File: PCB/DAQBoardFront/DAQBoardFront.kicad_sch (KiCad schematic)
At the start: 35 parts, among them IC2 LMR51430YDDCR, J2 53375-0410, U5 TCAN1051VDRQ1

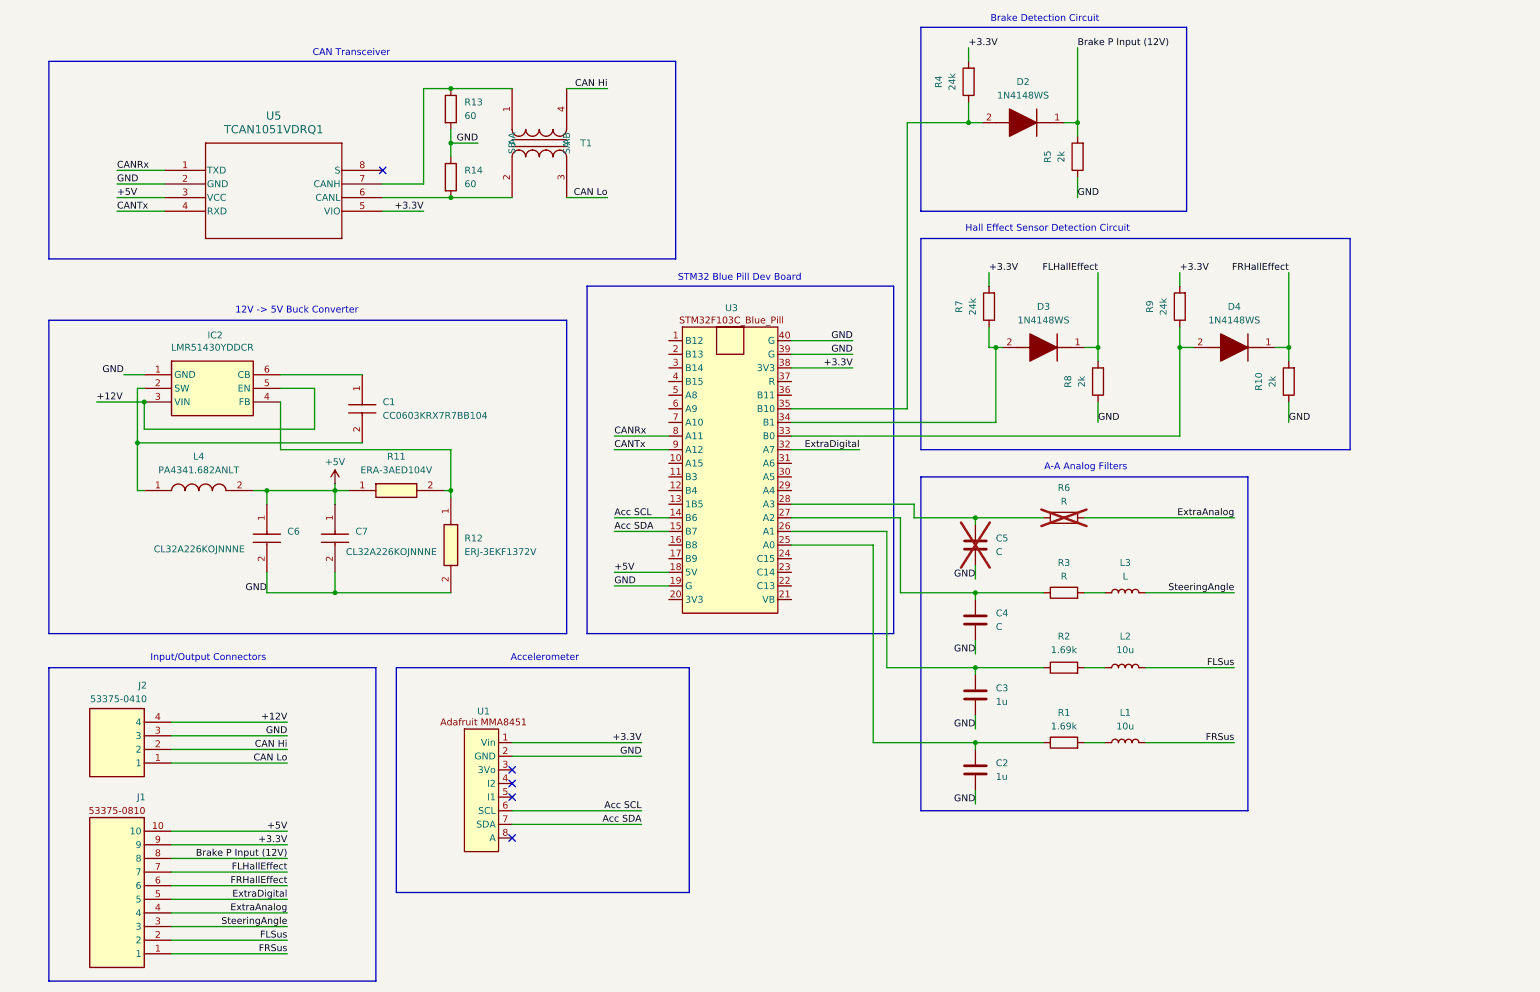
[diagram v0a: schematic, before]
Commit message: Added schematic design for current sense amplifier
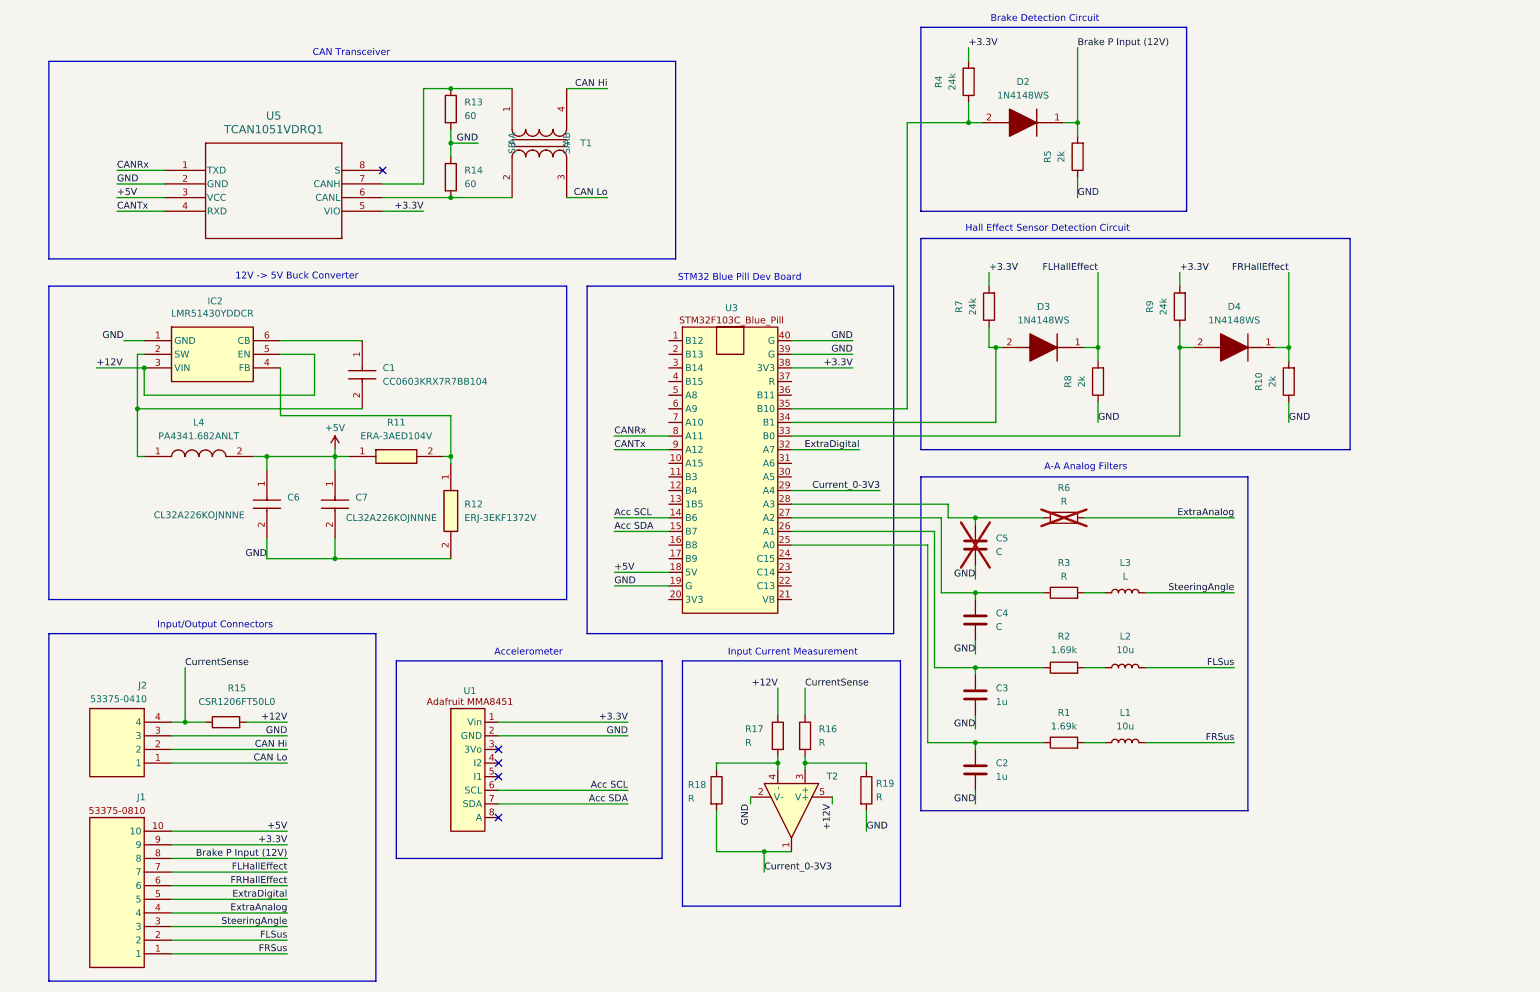
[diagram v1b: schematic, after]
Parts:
- added R15: CSR1206FT50L0, symbol Device:R
- added R16, R17, R18, R19: R, symbol Device:R
- added T2: (no value), CFR-Footprint-Library:NCS2005SN1T1G, symbol CFR Library:NCS2005SN1T1G
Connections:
- net +12V: now also R15.2, R17.1, T2.5 (V+); no longer J2.4
- net GND: now also R19.2, T2.2 (V-)
- net Current_0-3V3: now reaches U3.29 (A4)
- net Current_0-3V3: now also R18.2, T2.1
- new net: R16.2, R19.1, T2.3 (+)
- new net: R17.2, R18.1, T2.4 (-)
- new net CurrentSense: J2.4, R15.1, R16.1
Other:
- note added: "Input Current Measurement"
- moved on the sheet: C1, C6, C7, IC2, L4, R11, R12, U1

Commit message: Completed V2.0 of DAQ board, including buck converter, input current measurement, and onboard CAN Transceiver
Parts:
- added C8: C3216X5R1E476M160AC, Capacitor_SMD:C_1206_3216Metric_Pad1.33x1.80mm_HandSolder, symbol Device:C
- R15: footprint (none) -> Resistor_SMD:R_1206_3216Metric
- R16, R17: value R -> 100k; footprint (none) -> Resistor_SMD:R_0402_1005Metric
- R18: value R -> 22.1k; footprint (none) -> Resistor_SMD:R_0402_1005Metric
- R19: value R -> 56.2k; footprint (none) -> Resistor_SMD:R_0402_1005Metric
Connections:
- net +12V: now also C8.2
- net GND: now also C8.1
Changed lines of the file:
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@@
 	)
 	(junction
+		(at 25.4 82.55)
+		(diameter 0)
+		(color 0 0 0 0)
+	)
+	(junction
 		(at 68.58 96.52)
 		(diameter 0)
@@
 	)
 	(junction
-		(at 33.02 80.01)
+		(at 25.4 74.93)
 		(diameter 0)
 		(color 0 0 0 0)
@@
 	)
 	(junction
+		(at 33.02 82.55)
+		(diameter 0)
+		(color 0 0 0 0)
+	)
+	(junction
 		(at 90.17 96.52)
 		(diameter 0)
@@
 	(wire
 		(pts
+			(xy 25.4 74.93) (xy 33.02 74.93)
+		)
+		(stroke
+			(width 0)
+			(type default)
+		)
+	)
+	(wire
+		(pts
 			(xy 38.1 171.45) (xy 59.69 171.45)
 		)
@@
 	(wire
 		(pts
-			(xy 29.21 74.93) (xy 33.02 74.93)
+			(xy 17.78 74.93) (xy 25.4 74.93)
 		)
 		(stroke
@@
 	(wire
 		(pts
+			(xy 33.02 82.55) (xy 33.02 80.01)
+		)
+		(stroke
+			(width 0)
+			(type default)
+		)
+	)
+	(wire
+		(pts
 			(xy 85.09 45.72) (xy 77.47 45.72)
 		)
@@
 	(wire
 		(pts
-			(xy 33.02 80.01) (xy 24.13 80.01)
+			(xy 25.4 88.9) (xy 17.78 88.9)
 		)
 		(stroke
@@
 	(wire
 		(pts
+			(xy 33.02 82.55) (xy 33.02 85.09)
+		)
+		(stroke
+			(width 0)
+			(type default)
+		)
+	)
+	(wire
+		(pts
 			(xy 180.34 135.89) (xy 187.96 135.89)
 		)
@@
 	(wire
 		(pts
-			(xy 33.02 85.09) (xy 33.02 80.01)
-		)
-		(stroke
-			(width 0)
-			(type default)
-		)
-	)
-	(wire
-		(pts
 			(xy 187.96 107.95) (xy 187.96 109.22)
 		)
@@
 	(wire
 		(pts
+			(xy 25.4 88.9) (xy 25.4 82.55)
+		)
+		(stroke
+			(width 0)
+			(type default)
+		)
+	)
+	(wire
+		(pts
 			(xy 146.05 161.29) (xy 146.05 160.02)
 		)
@@
 	(wire
 		(pts
+			(xy 25.4 82.55) (xy 33.02 82.55)
+		)
+		(stroke
+			(width 0)
+			(type default)
+		)
+	)
+	(wire
+		(pts
 			(xy 58.42 74.93) (xy 73.66 74.93)
 		)
@@
 	)
 	(label "GND"
-		(at 29.21 74.93 180)
+		(at 17.78 74.93 0)
 		(effects
 			(font
 				(size 1.27 1.27)
 			)
-			(justify right bottom)
+			(justify left bottom)
 		)
 	)
@@
 	)
 	(label "+12V"
-		(at 24.13 80.01 0)
+		(at 17.78 88.9 0)
 		(effects
 			(font
@@
 	)
 	(label "GND"
-		(at 167.64 166.37 0)
+		(at 167.64 166.37 270)
 		(effects
 			(font
 				(size 1.27 1.27)
 			)
-			(justify left bottom)
+			(justify right bottom)
 		)
 	)
@@
 			)
 		)
-		(property "Value" "R"
+		(property "Value" "100k"
 			(at 158.75 149.8599 0)
 			(show_name no)
@@
 			)
 		)
-		(property "Footprint" ""
+		(property "Footprint" "Resistor_SMD:R_0402_1005Metric"
 			(at 154.432 148.59 90)
 			(hide yes)
@@
 			)
 		)
-		(property "Value" "R"
-			(at 169.418 160.02 0)
+		(property "Value" "56.2k"
+			(at 170.942 164.338 90)
 			(show_name no)
 			(do_not_autoplace no)
@@
 			)
 		)
-		(property "Footprint" ""
+		(property "Footprint" "Resistor_SMD:R_0402_1005Metric"
 			(at 165.862 158.75 90)
 			(hide yes)
@@
 			)
 		)
-		(property "Value" "R"
-			(at 134.366 160.274 0)
+		(property "Value" "22.1k"
+			(at 137.16 164.592 90)
 			(show_name no)
 			(do_not_autoplace no)
@@
 			)
 		)
-		(property "Footprint" ""
+		(property "Footprint" "Resistor_SMD:R_0402_1005Metric"
 			(at 137.922 158.75 90)
 			(hide yes)
@@
 			)
 		)
-		(property "Value" "R"
+		(property "Value" "100k"
 			(at 145.034 149.86 0)
 			(show_name no)
@@
 			)
 		)
-		(property "Footprint" ""
+		(property "Footprint" "Resistor_SMD:R_0402_1005Metric"
 			(at 149.352 148.59 90)
 			(hide yes)
@@
 			)
 		)
-		(property "Footprint" ""
+		(property "Footprint" "Resistor_SMD:R_1206_3216Metric"
 			(at 48.26 147.828 90)
 			(hide yes)
@@
 					(unit 1)
 				)
+			)
+		)
+	)
+	(symbol
+		(lib_id "Device:C")
+		(at 25.4 78.74 0)
+		(unit 1)
+		(body_style 1)
+		(exclude_from_sim no)
+		(in_bom yes)
+		(on_board yes)
+		(in_pos_files yes)
+		(dnp no)
+		(property "Reference" "C8"
+			(at 28.194 77.47 0)
+			(show_name no)
+			(do_not_autoplace no)
+			(effects
+				(font
+					(size 1.27 1.27)
+				)
+				(justify left)
+			)
+		)
+		(property "Value" "C3216X5R1E476M160AC"
+			(at 8.128 81.28 0)
+			(show_name no)
+			(do_not_autoplace no)
+			(effects
+				(font
+					(size 1.27 1.27)
+				)
+				(justify left)
+			)
+		)
+		(property "Footprint" "Capacitor_SMD:C_1206_3216Metric_Pad1.33x1.80mm_HandSolder"
+			(at 26.3652 82.55 0)
+			(hide yes)
+			(show_name no)
+			(do_not_autoplace no)
+			(effects
+				(font
+					(size 1.27 1.27)
+				)
+			)
+		)
+		(property "Datasheet" ""
+			(at 25.4 78.74 0)
+			(hide yes)
+			(show_name no)
+			(do_not_autoplace no)
+			(effects
+				(font
+					(size 1.27 1.27)
+				)
+			)
+		)
+		(property "Description" "Unpolarized capacitor"
+			(at 25.4 78.74 0)
+			(hide yes)
+			(show_name no)
+			(do_not_autoplace no)
+			(effects
+				(font
+					(size 1.27 1.27)
+				)
+			)
+		)
+		(pin "2"
+		)
+		(pin "1"
+		)
+		(instances
+			(project "DAQBoardFront"
+				(path "/b8c14199-b7a8-42b0-9649-393d2e0c6b59"
+					(reference "C8")
+					(unit 1)
+				)

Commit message: V1.0 of dashboard, plus minor changes to DAQ board
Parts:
- J1, J2, T1, U1, U3: now not fitted
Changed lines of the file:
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@@
 		(on_board yes)
 		(in_pos_files yes)
-		(dnp no)
+		(dnp yes)
 		(property "Reference" "J2"
 			(at 33.528 139.192 0)
@@
 		(on_board yes)
 		(in_pos_files yes)
-		(dnp no)
+		(dnp yes)
 		(property "Reference" "U1"
 			(at 93.726 140.208 0)
@@
 		(on_board yes)
 		(in_pos_files yes)
-		(dnp no)
+		(dnp yes)
 		(property "Reference" "T1"
 			(at 114.3 38.1 90)
@@
 		(on_board yes)
 		(in_pos_files yes)
-		(dnp no)
+		(dnp yes)
 		(property "Reference" "U3"
 			(at 142.494 68.834 0)
@@
 		(on_board yes)
 		(in_pos_files yes)
-		(dnp no)
+		(dnp yes)
 		(property "Reference" "J1"
 			(at 33.274 160.02 0)

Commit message: Updated BOM and place files for DAQ Board
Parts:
- C8: value C3216X5R1E476M160AC -> C3216X5R1E476MTJ00E
- R13, R14: now not fitted
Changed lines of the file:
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@@
 		(on_board yes)
 		(in_pos_files yes)
-		(dnp no)
+		(dnp yes)
 		(fields_autoplaced yes)
 		(property "Reference" "R13"
@@
 			)
 		)
-		(property "Description" "Resistor, 60Ohm, 1%, 1/4W"
+		(property "Description" "RCS060359R0FKEA"
 			(at 90.17 31.75 0)
 			(hide yes)
@@
 		(on_board yes)
 		(in_pos_files yes)
-		(dnp no)
+		(dnp yes)
 		(fields_autoplaced yes)
 		(property "Reference" "R14"
@@
 			)
 		)
-		(property "Description" "Resistor, 60Ohm, 1%, 1/4W"
+		(property "Description" "RCS060359R0FKEA"
 			(at 90.17 44.45 0)
 			(hide yes)
@@
 			)
 		)
-		(property "Value" "C3216X5R1E476M160AC"
+		(property "Value" "C3216X5R1E476MTJ00E"
 			(at 8.128 81.28 0)
 			(show_name no)

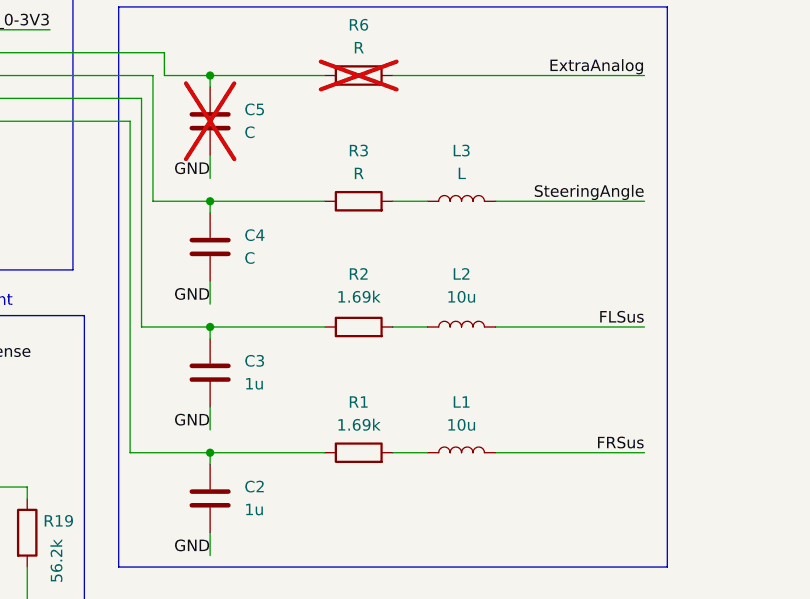
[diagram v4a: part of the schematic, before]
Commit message: Updated A-A filters w/ final version, updated BOM
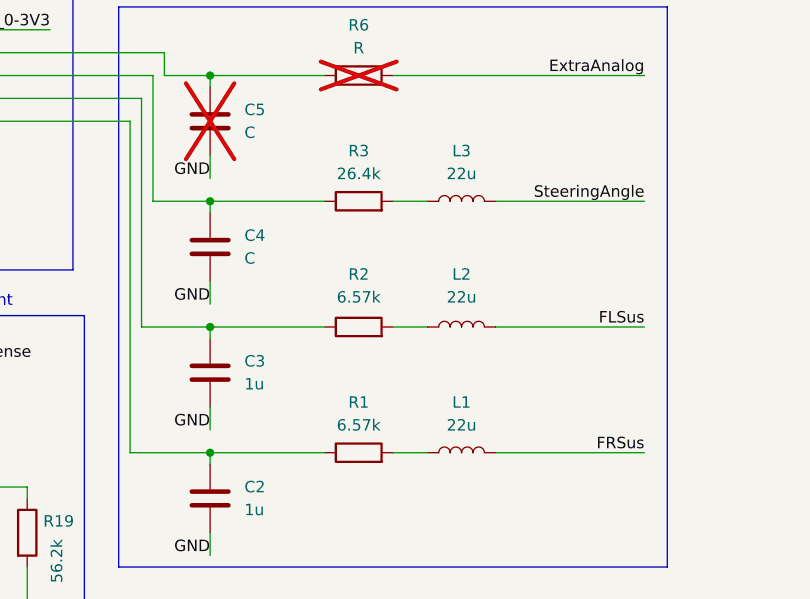
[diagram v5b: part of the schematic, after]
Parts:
- L1, L2: value 10u -> 22u
- L3: value L -> 22u
- R1, R2: value 1.69k -> 6.57k
- R3: value R -> 26.4k
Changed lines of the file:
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@@
 			)
 		)
-		(property "Value" "10u"
+		(property "Value" "22u"
 			(at 215.9 132.588 90)
 			(show_name no)
@@
 			)
 		)
-		(property "Value" "L"
+		(property "Value" "22u"
 			(at 215.9 118.872 90)
 			(show_name no)
@@
 			)
 		)
-		(property "Value" "10u"
+		(property "Value" "22u"
 			(at 215.9 146.812 90)
 			(show_name no)
@@
 			)
 		)
-		(property "Value" "1.69k"
+		(property "Value" "6.57k"
 			(at 204.47 132.588 90)
 			(show_name no)
@@
 			)
 		)
-		(property "Value" "R"
+		(property "Value" "26.4k"
 			(at 204.47 118.872 90)
 			(show_name no)
@@
 			)
 		)
-		(property "Value" "1.69k"
+		(property "Value" "6.57k"
 			(at 204.47 146.812 90)
 			(show_name no)
